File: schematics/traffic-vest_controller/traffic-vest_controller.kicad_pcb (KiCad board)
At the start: 2 copper layers, 41.4 x 83.8 mm, 29 parts

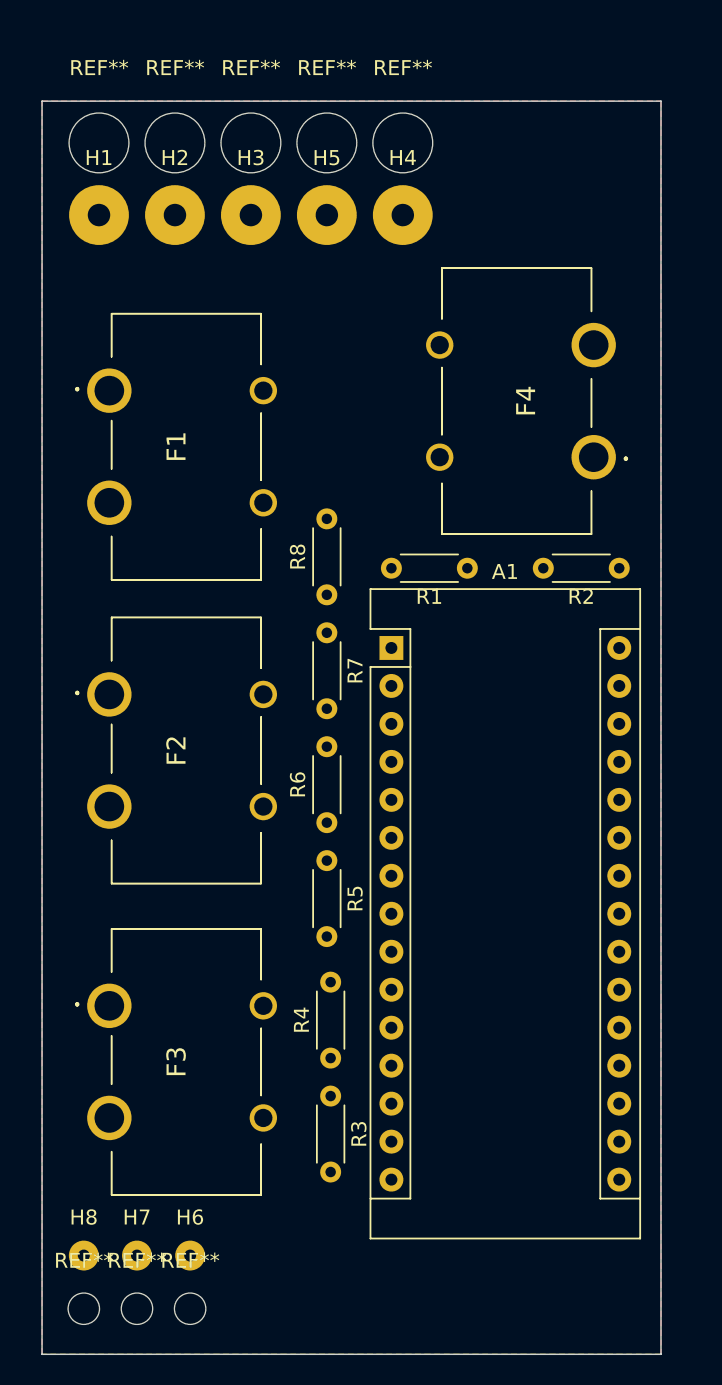
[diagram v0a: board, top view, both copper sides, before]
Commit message: expanded board footprint to accomodate corner mounting holes; rearranged fuses and pins for left/right to D2, D3 for external interrupts; fixed orientation of fuse clips
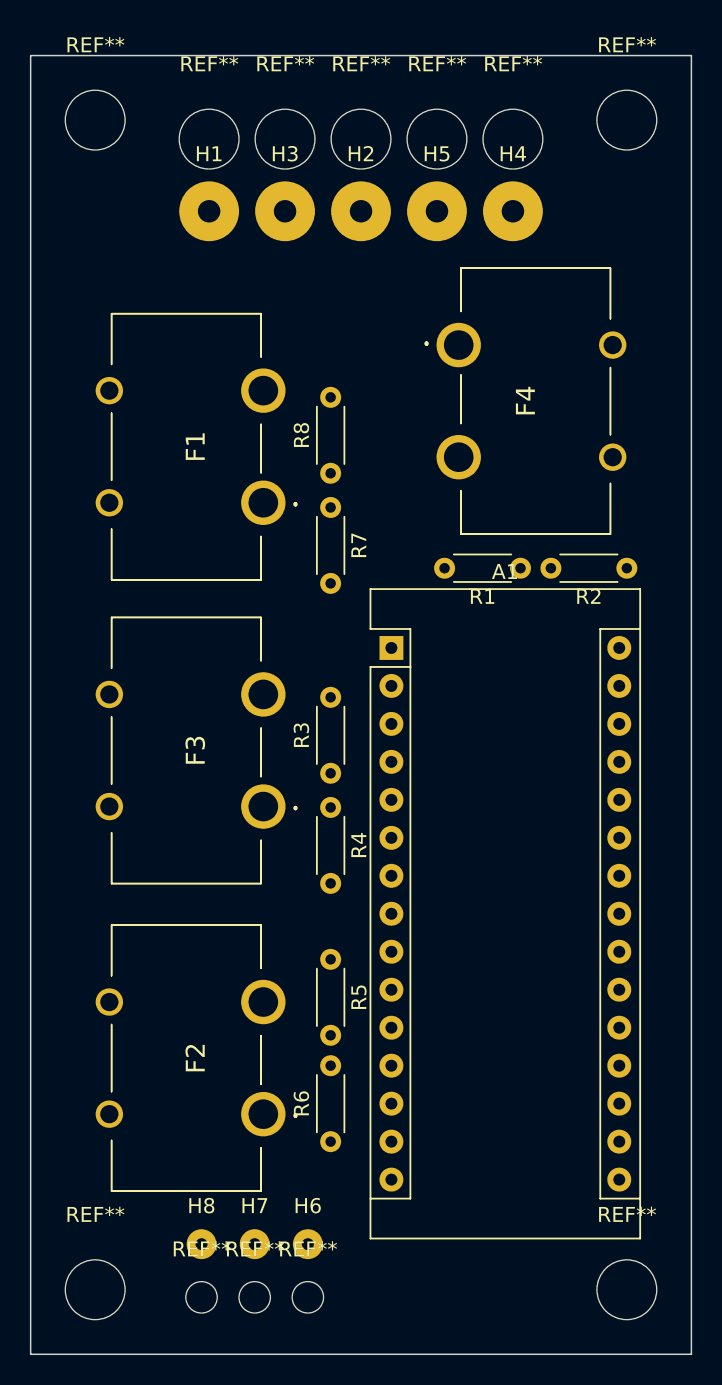
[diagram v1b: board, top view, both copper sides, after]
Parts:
- added REF**: MountingHole_4mm, MountingHole:MountingHole_4mm, F.Cu at (92.5, 124.0)
- added REF**: MountingHole_4mm, MountingHole:MountingHole_4mm, F.Cu at (56.9, 124.0)
- added REF**: MountingHole_4mm, MountingHole:MountingHole_4mm, F.Cu at (56.9, 45.7)
- added REF**: MountingHole_4mm, MountingHole:MountingHole_4mm, F.Cu at (92.5, 45.7)
- moved R3 21.6 mm to (72.6, 89.4), turned to 90 degrees
- moved R6 21.3 mm to (72.6, 114.0)
- moved F3 20.8 mm to (63.0, 87.9), turned to 90 degrees
- moved F2 20.6 mm to (63.0, 108.5), turned to 90 degrees
- moved R4 16.8 mm to (72.6, 91.7), turned to 270 degrees
- moved H2 12.4 mm to (74.7, 51.8)
- moved R7 8.39 mm to (72.6, 71.6)
- moved R8 8.13 mm to (72.6, 69.3)
- moved H6 7.91 mm to (71.1, 120.9)
- moved REF** 7.91 mm to (71.1, 124.5)
- moved H7 7.91 mm to (67.6, 120.9)
- moved H8 7.91 mm to (64.0, 120.9)
- moved REF** 7.91 mm to (67.6, 124.5)
- moved REF** 7.91 mm to (64.0, 124.5)
- moved H1 7.37 mm to (64.5, 51.8)
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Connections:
- H1 pad 1: Net-(F1-Pad1) -> Net-(F1-Pad3)
- H2 pad 1: Net-(F2-Pad1) -> Net-(F2-Pad4)
- H3 pad 1: Net-(F3-Pad1) -> Net-(F3-Pad4)
- H4 pad 1: Net-(F4-Pad2) -> Net-(F4-Pad1)
- H6 pad 1: Net-(F4-Pad1) -> Net-(F4-Pad2)
- R1 pad 2: Net-(F4-Pad1) -> Net-(F4-Pad2)
- R3 pad 1: Net-(A1-Pad14) -> Net-(A1-Pad6)
- R3 pad 2: Net-(F3-Pad3) -> Net-(F3-Pad2)
- R4 pad 1: Net-(A1-Pad14) -> Net-(A1-Pad6)
- R5 pad 1: Net-(A1-Pad7) -> Net-(A1-Pad14)
- R5 pad 2: Net-(F2-Pad3) -> Net-(F2-Pad2)
- R6 pad 1: Net-(A1-Pad7) -> Net-(A1-Pad14)
- R7 pad 2: Net-(F1-Pad3) -> Net-(F1-Pad1)
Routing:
- removed copper zone on F.Cu, net GNDREF
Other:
- board size 41.4 x 83.8 mm -> 44.2 x 86.9 mm

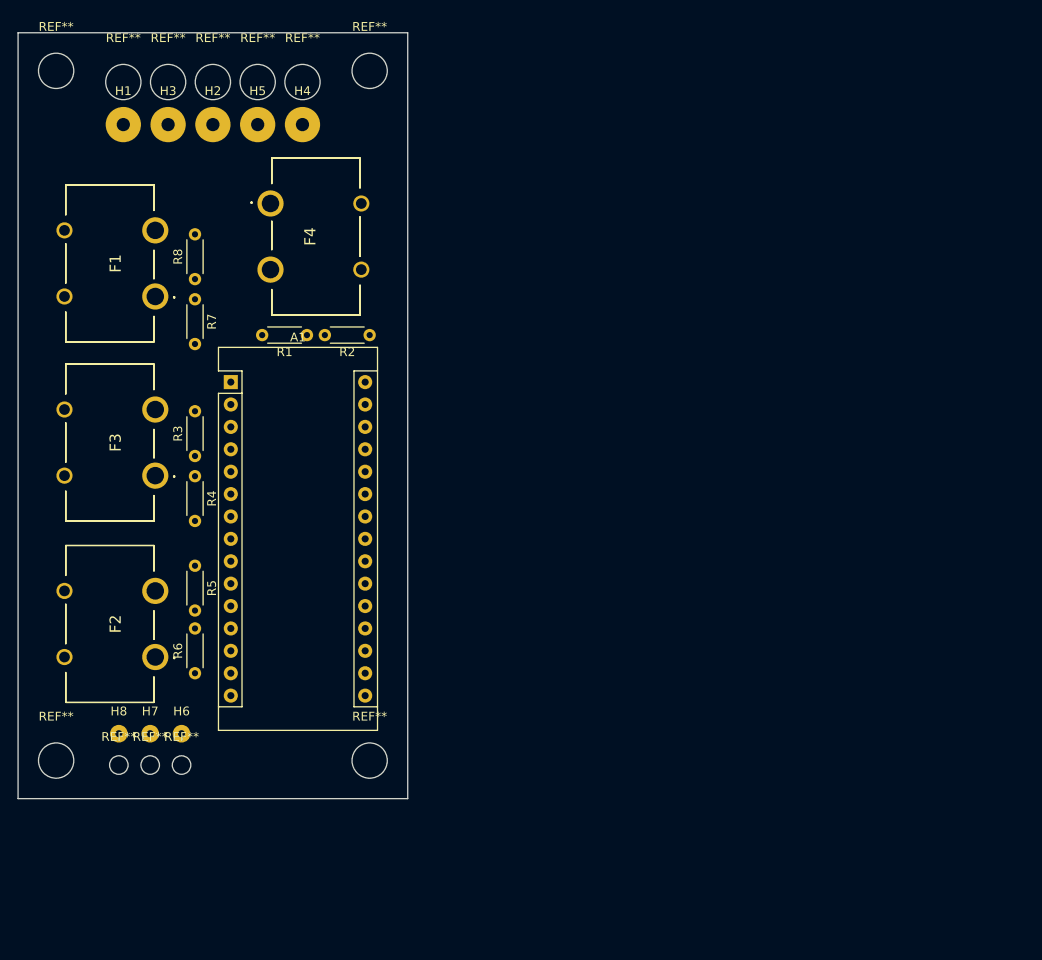
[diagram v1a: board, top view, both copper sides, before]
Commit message: Routed tracks and added ground pour.  Potentially finished PCB layout!
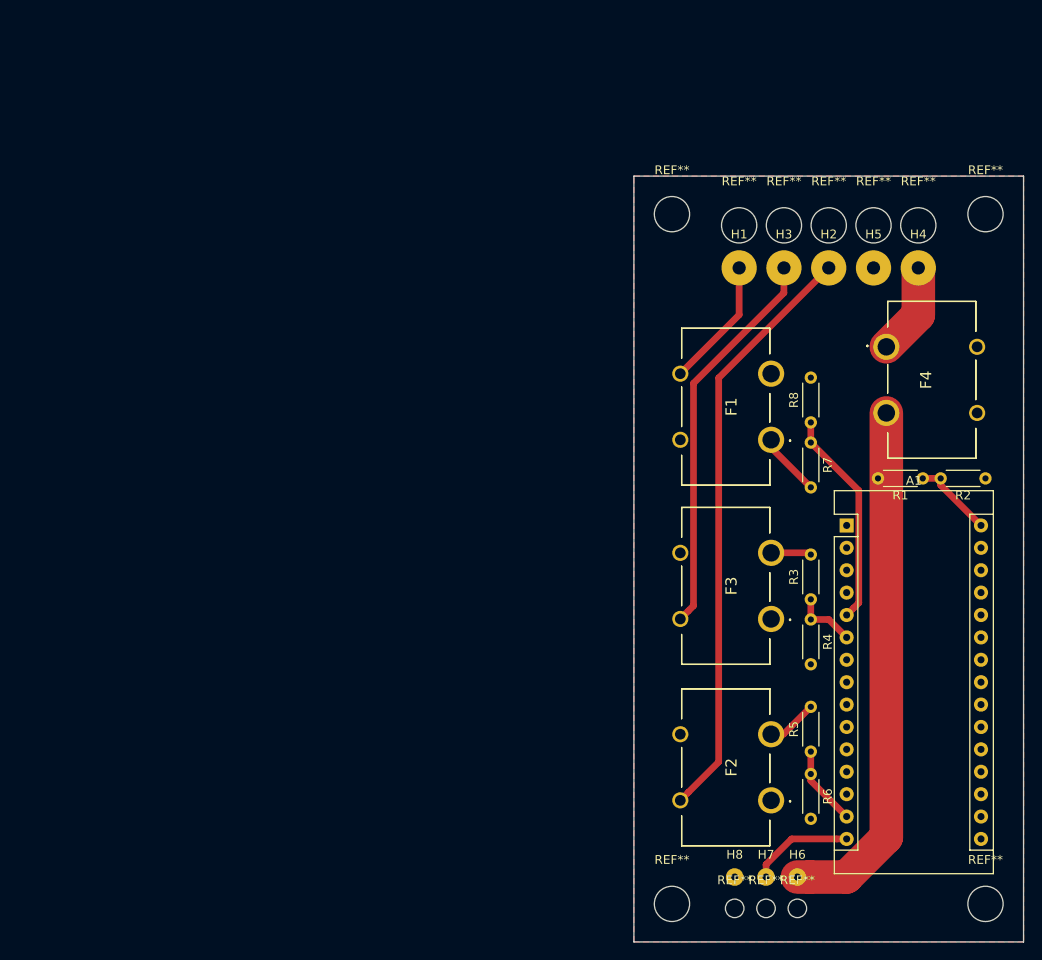
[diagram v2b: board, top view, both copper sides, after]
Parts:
- moved R5 73.0 mm to (142.5, 122.9), turned to 90 degrees
- moved F1 71.7 mm to (132.8, 83.8)
- moved F2 71.7 mm to (132.8, 124.7)
- moved F3 71.7 mm to (132.8, 104.1)
- moved F4 71.7 mm to (156.2, 80.8)
- moved H1 71.7 mm to (134.4, 68.1)
- moved H2 71.7 mm to (144.5, 68.1)
- moved H4 71.7 mm to (154.7, 68.1)
- moved H8 71.7 mm to (133.9, 137.2)
- moved R2 71.7 mm to (162.3, 91.9)
- moved REF** 71.7 mm to (162.3, 140.2)
- moved REF** 71.7 mm to (133.9, 140.7)
- moved REF** 71.7 mm to (162.3, 62.0)
- moved REF** 71.7 mm to (144.5, 63.2)
- moved REF** 71.7 mm to (134.4, 63.2)
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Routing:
- net Net-(F2-Pad4): track 0.00 -> 67.4 mm
- net Net-(F4-Pad2): track 0.00 -> 60.1 mm
- net Net-(F3-Pad4): track 0.00 -> 44.7 mm
- net Net-(A1-Pad5): track 0.00 -> 24.7 mm
- net Net-(F1-Pad3): track 0.00 -> 14.8 mm
- net Net-(A1-Pad15): track 0.00 -> 11.8 mm
- net Net-(F4-Pad1): track 0.00 -> 10.5 mm
- net Net-(A1-Pad30): track 0.00 -> 9.26 mm
- net Net-(A1-Pad14): track 0.00 -> 9.05 mm
- net Net-(F1-Pad1): track 0.00 -> 7.26 mm
- net Net-(A1-Pad6): track 0.00 -> 7.19 mm
- net Net-(F2-Pad2): track 0.00 -> 5.79 mm
- net Net-(F3-Pad2): track 0.00 -> 4.58 mm
- added copper zone on F.Cu, net GNDREF
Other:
- net class Default: clearance 0.2 -> 0.381
- rule trace_clearance: 0.2 -> 0.381

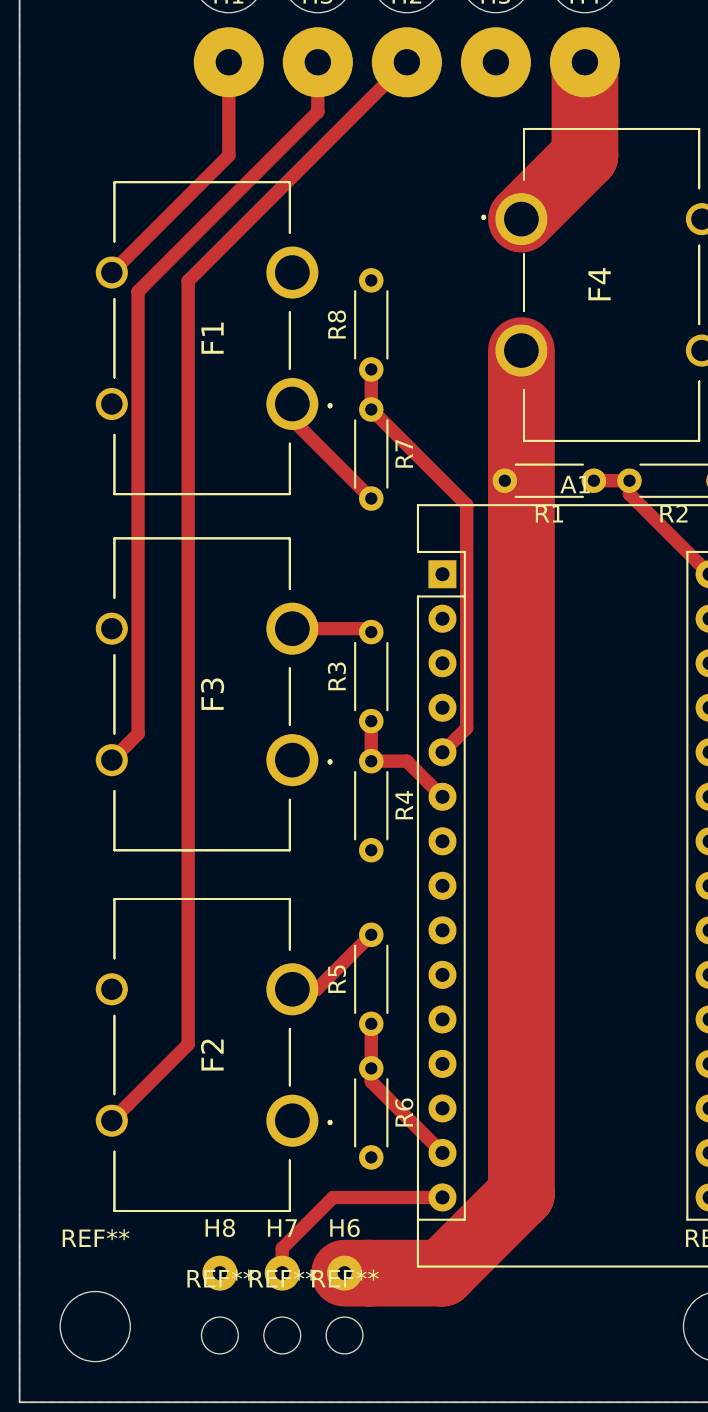
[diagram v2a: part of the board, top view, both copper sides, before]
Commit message: Minor track tweaks
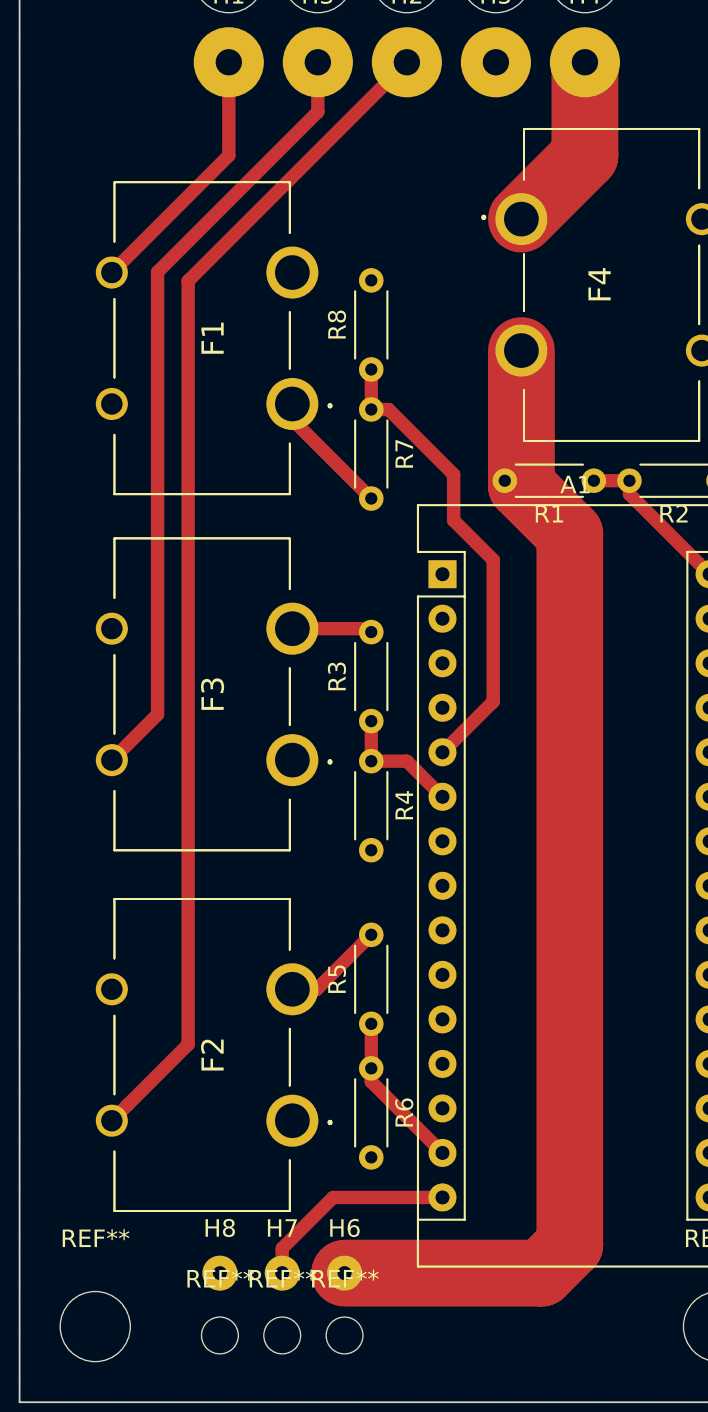
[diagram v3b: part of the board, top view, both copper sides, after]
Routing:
- net Net-(F4-Pad2): track 60.1 -> 65.7 mm
- net Net-(A1-Pad5): track 24.7 -> 26.5 mm
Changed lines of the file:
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@@
     (thickness 1.6)
     (drawings 6)
-    (tracks 41)
+    (tracks 44)
     (zones 0)
     (modules 33)
@@
   (segment (start 142.494 107.95) (end 144.526 107.95) (width 0.762) (layer F.Cu) (net 20))
   (segment (start 142.494 85.598) (end 142.494 87.884) (width 0.762) (layer F.Cu) (net 22))
-  (segment (start 147.357999 106.642001) (end 146.558 107.442) (width 0.762) (layer F.Cu) (net 22))
-  (segment (start 147.939001 106.060999) (end 147.357999 106.642001) (width 0.762) (layer F.Cu) (net 22))
-  (segment (start 147.939001 93.329001) (end 147.939001 106.060999) (width 0.762) (layer F.Cu) (net 22))
-  (segment (start 142.494 87.884) (end 147.939001 93.329001) (width 0.762) (layer F.Cu) (net 22))
+  (segment (start 143.483949 87.884) (end 147.193 91.593051) (width 0.762) (layer F.Cu) (net 22))
+  (segment (start 142.494 87.884) (end 143.483949 87.884) (width 0.762) (layer F.Cu) (net 22))
+  (segment (start 147.193 91.593051) (end 147.193 94.2086) (width 0.762) (layer F.Cu) (net 22))
+  (segment (start 147.193 94.2086) (end 149.4536 96.4692) (width 0.762) (layer F.Cu) (net 22))
+  (segment (start 149.4536 104.5464) (end 149.4028 104.5972) (width 0.762) (layer F.Cu) (net 22))
+  (segment (start 149.4536 96.4692) (end 149.4536 104.5464) (width 0.762) (layer F.Cu) (net 22))
+  (segment (start 149.4028 104.5972) (end 146.558 107.442) (width 0.762) (layer F.Cu) (net 22))
   (segment (start 134.366 73.396) (end 127.692 80.07) (width 0.762) (layer F.Cu) (net 31))
   (segment (start 134.366 68.072) (end 134.366 73.396) (width 0.762) (layer F.Cu) (net 31))
@@
   (segment (start 139.386 120.964) (end 142.494 117.856) (width 0.762) (layer F.Cu) (net 35))
   (segment (start 137.992 120.964) (end 139.386 120.964) (width 0.762) (layer F.Cu) (net 35))
-  (segment (start 128.606999 106.975001) (end 127.692 107.89) (width 0.762) (layer F.Cu) (net 36))
-  (segment (start 129.188001 106.393999) (end 128.606999 106.975001) (width 0.762) (layer F.Cu) (net 36))
-  (segment (start 129.188001 81.158779) (end 129.188001 106.393999) (width 0.762) (layer F.Cu) (net 36))
-  (segment (start 139.446 70.90078) (end 129.188001 81.158779) (width 0.762) (layer F.Cu) (net 36))
+  (segment (start 139.446 70.90078) (end 130.302 80.04478) (width 0.762) (layer F.Cu) (net 36))
   (segment (start 139.446 68.072) (end 139.446 70.90078) (width 0.762) (layer F.Cu) (net 36))
+  (segment (start 130.302 105.28) (end 127.692 107.89) (width 0.762) (layer F.Cu) (net 36))
+  (segment (start 130.302 80.04478) (end 130.302 105.28) (width 0.762) (layer F.Cu) (net 36))
   (segment (start 142.3 100.39) (end 142.494 100.584) (width 0.762) (layer F.Cu) (net 38))
   (segment (start 137.992 100.39) (end 142.3 100.39) (width 0.762) (layer F.Cu) (net 38))
-  (segment (start 142.383492 137.16) (end 140.97 137.16) (width 3.81) (layer F.Cu) (net 41))
-  (segment (start 146.539402 137.16) (end 142.383492 137.16) (width 3.81) (layer F.Cu) (net 41))
-  (segment (start 151.06 132.639402) (end 146.539402 137.16) (width 3.81) (layer F.Cu) (net 41))
-  (segment (start 151.06 84.522) (end 151.06 132.639402) (width 3.81) (layer F.Cu) (net 41))
+  (segment (start 152.1968 137.16) (end 140.97 137.16) (width 3.81) (layer F.Cu) (net 41))
+  (segment (start 153.8224 94.995682) (end 153.8224 135.5344) (width 3.81) (layer F.Cu) (net 41))
+  (segment (start 153.8224 135.5344) (end 152.1968 137.16) (width 3.81) (layer F.Cu) (net 41))
+  (segment (start 151.06 92.233282) (end 153.8224 94.995682) (width 3.81) (layer F.Cu) (net 41))
+  (segment (start 151.06 84.522) (end 151.06 92.233282) (width 3.81) (layer F.Cu) (net 41))
   (segment (start 137.992 88.462) (end 142.494 92.964) (width 0.762) (layer F.Cu) (net 42))
   (segment (start 137.992 87.57) (end 137.992 88.462) (width 0.762) (layer F.Cu) (net 42))
